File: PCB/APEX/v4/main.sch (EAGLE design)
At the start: 24 parts

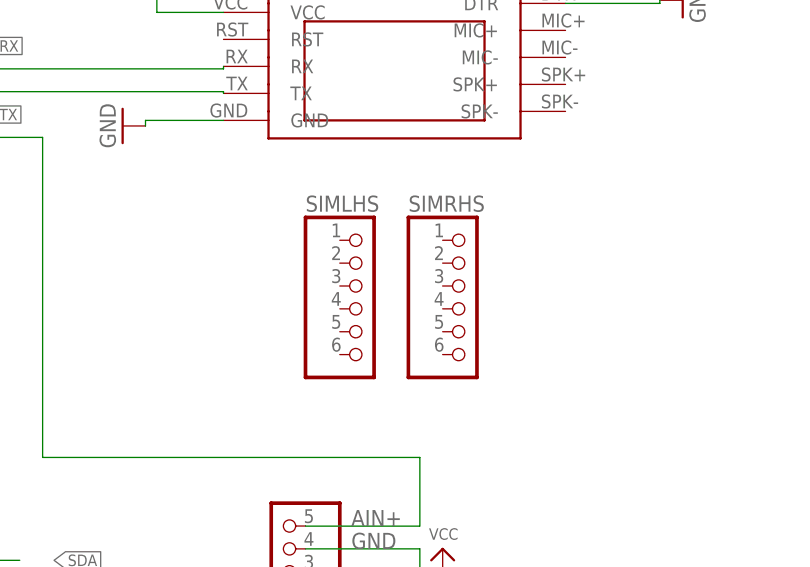
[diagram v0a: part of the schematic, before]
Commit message: use drc to increase pad size
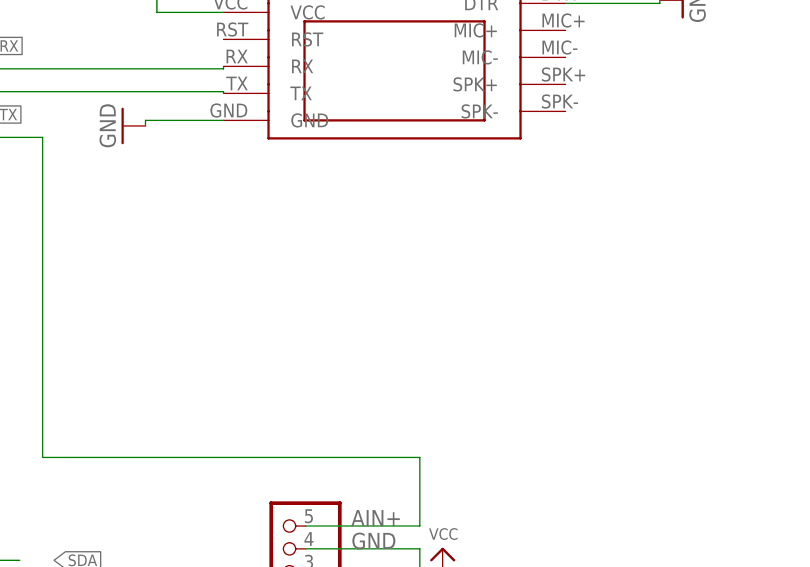
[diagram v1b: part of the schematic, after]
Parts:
- removed SIMLHS, SIMRHS: (no value), pinhead:PINHD-1X6
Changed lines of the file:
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@@
 <part name="TINYLHS" library="pinhead" library_urn="urn:adsk.eagle:library:325" deviceset="PINHD-1X8" device="" package3d_urn="urn:adsk.eagle:package:22409/2"/>
 <part name="TINYRHS" library="pinhead" library_urn="urn:adsk.eagle:library:325" deviceset="PINHD-1X8" device="" package3d_urn="urn:adsk.eagle:package:22409/2"/>
-<part name="SIMLHS" library="pinhead" library_urn="urn:adsk.eagle:library:325" deviceset="PINHD-1X6" device="" package3d_urn="urn:adsk.eagle:package:22472/2"/>
-<part name="SIMRHS" library="pinhead" library_urn="urn:adsk.eagle:library:325" deviceset="PINHD-1X6" device="" package3d_urn="urn:adsk.eagle:package:22472/2"/>
 <part name="EXTV+" library="wirepad" library_urn="urn:adsk.eagle:library:412" deviceset="SMD5" device="" package3d_urn="urn:adsk.eagle:package:30841/1"/>
 <part name="EXTGND" library="wirepad" library_urn="urn:adsk.eagle:library:412" deviceset="SMD5" device="" package3d_urn="urn:adsk.eagle:package:30841/1"/>
@@
 <attribute name="VALUE" x="-6.35" y="45.72" size="1.778" layer="96"/>
 </instance>
-<instance part="SIMLHS" gate="A" x="95.25" y="33.02" smashed="yes">
-<attribute name="NAME" x="88.9" y="43.815" size="1.778" layer="95"/>
-<attribute name="VALUE" x="88.9" y="22.86" size="1.778" layer="96"/>
-</instance>
-<instance part="SIMRHS" gate="A" x="106.68" y="33.02" smashed="yes">
-<attribute name="NAME" x="100.33" y="43.815" size="1.778" layer="95"/>
-<attribute name="VALUE" x="100.33" y="22.86" size="1.778" layer="96"/>
-</instance>
 <instance part="EXTV+" gate="1" x="-21.59" y="17.78" smashed="yes">

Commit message: transfer changes to parent file
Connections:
- net AIN+: now also TINYLHS.8
- net GND: now also TINYRHS.2, TINYRHS.8
- net RX: now also TINYLHS.5
- net SCL: now also TINYRHS.6
- net SDA: now also TINYRHS.7
- net TX: now also TINYLHS.6
- net VCC: now also TINYRHS.1
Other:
- moved on the sheet: TINYLHS, TINYRHS
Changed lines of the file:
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@@
 <setting verticaltext="up"/>
 </settings>
-<grid distance="0.05" unitdist="inch" unit="inch" style="lines" multiple="1" display="yes" altdistance="0.005" altunitdist="inch" altunit="inch"/>
+<grid distance="0.1" unitdist="inch" unit="inch" style="lines" multiple="1" display="no" altdistance="0.01" altunitdist="inch" altunit="inch"/>
 <layers>
 <layer number="1" name="Top" color="4" fill="1" visible="no" active="no"/>
@@
 <attribute name="VALUE" x="-1.27" y="80.01" size="1.778" layer="96"/>
 </instance>
-<instance part="TINYLHS" gate="A" x="-10.16" y="58.42" smashed="yes">
-<attribute name="NAME" x="-16.51" y="71.755" size="1.778" layer="95"/>
-<attribute name="VALUE" x="-16.51" y="45.72" size="1.778" layer="96"/>
-</instance>
-<instance part="TINYRHS" gate="A" x="0" y="58.42" smashed="yes">
-<attribute name="NAME" x="-6.35" y="71.755" size="1.778" layer="95"/>
-<attribute name="VALUE" x="-6.35" y="45.72" size="1.778" layer="96"/>
+<instance part="TINYLHS" gate="A" x="115.57" y="29.21" smashed="yes">
+<attribute name="NAME" x="109.22" y="42.545" size="1.778" layer="95"/>
+<attribute name="VALUE" x="109.22" y="16.51" size="1.778" layer="96"/>
+</instance>
+<instance part="TINYRHS" gate="A" x="-21.59" y="58.42" smashed="yes">
+<attribute name="NAME" x="-27.94" y="71.755" size="1.778" layer="95"/>
+<attribute name="VALUE" x="-27.94" y="45.72" size="1.778" layer="96"/>
 </instance>
 <instance part="EXTV+" gate="1" x="-21.59" y="17.78" smashed="yes">
@@
 <wire x1="231.14" y1="13.97" x2="242.57" y2="13.97" width="0.1524" layer="91"/>
 </segment>
+<segment>
+<pinref part="TINYRHS" gate="A" pin="1"/>
+<wire x1="-24.13" y1="68.58" x2="-34.29" y2="68.58" width="0.1524" layer="91"/>
+<label x="-39.37" y="68.58" size="1.27" layer="95" rot="R180" xref="yes"/>
+</segment>
 </net>
 <net name="GND" class="0">
@@
 <wire x1="231.14" y1="7.62" x2="242.57" y2="7.62" width="0.1524" layer="91"/>
 </segment>
+<segment>
+<pinref part="TINYRHS" gate="A" pin="2"/>
+<wire x1="-24.13" y1="66.04" x2="-34.29" y2="66.04" width="0.1524" layer="91"/>
+<label x="-39.37" y="64.77" size="1.27" layer="95" rot="R180" xref="yes"/>
+</segment>
+<segment>
+<pinref part="TINYRHS" gate="A" pin="8"/>
+<wire x1="-24.13" y1="50.8" x2="-34.29" y2="50.8" width="0.1524" layer="91"/>
+<label x="-39.37" y="49.53" size="1.27" layer="95" rot="R180" xref="yes"/>
+</segment>
 </net>
 <net name="AIN+" class="0">
@@
 <wire x1="59.69" y1="52.07" x2="59.69" y2="16.51" width="0.1524" layer="91"/>
 <wire x1="59.69" y1="16.51" x2="101.6" y2="16.51" width="0.1524" layer="91"/>
+<wire x1="101.6" y1="16.51" x2="101.6" y2="21.59" width="0.1524" layer="91"/>
+<junction x="101.6" y="16.51"/>
+<pinref part="TINYLHS" gate="A" pin="8"/>
+<wire x1="101.6" y1="21.59" x2="113.03" y2="21.59" width="0.1524" layer="91"/>
 </segment>
 </net>
@@
 <label x="53.34" y="54.61" size="1.27" layer="95" xref="yes"/>
 </segment>
+<segment>
+<pinref part="TINYLHS" gate="A" pin="6"/>
+<wire x1="113.03" y1="26.67" x2="97.79" y2="26.67" width="0.1524" layer="91"/>
+<label x="93.98" y="26.67" size="1.27" layer="95" rot="R180" xref="yes"/>
+</segment>
 </net>
 <net name="RX" class="0">
@@
 <label x="53.34" y="62.23" size="1.27" layer="95" xref="yes"/>
 </segment>
+<segment>
+<pinref part="TINYLHS" gate="A" pin="5"/>
+<wire x1="113.03" y1="29.21" x2="97.79" y2="29.21" width="0.1524" layer="91"/>
+<label x="97.79" y="30.48" size="1.27" layer="95" rot="R90" xref="yes"/>
+</segment>
 </net>
 <net name="SDA" class="0">
@@
 <label x="252.73" y="-5.08" size="1.27" layer="95" xref="yes"/>
 </segment>
+<segment>
+<pinref part="TINYRHS" gate="A" pin="7"/>
+<wire x1="-24.13" y1="53.34" x2="-34.29" y2="53.34" width="0.1524" layer="91"/>
+<label x="-39.37" y="53.34" size="1.27" layer="95" rot="R180" xref="yes"/>
+</segment>
 </net>
 <net name="SCL" class="0">
@@
 <label x="252.73" y="1.27" size="1.27" layer="95" xref="yes"/>
 </segment>
+<segment>
+<pinref part="TINYRHS" gate="A" pin="6"/>
+<wire x1="-24.13" y1="55.88" x2="-34.29" y2="55.88" width="0.1524" layer="91"/>
+<label x="-39.37" y="57.15" size="1.27" layer="95" rot="R180" xref="yes"/>
+</segment>
 </net>

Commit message: backport changes to parent design
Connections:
- net SIMPOW: now also U$1.RST
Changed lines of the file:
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@@
 <label x="76.2" y="77.47" size="1.27" layer="95" xref="yes"/>
+</segment>
+<segment>
+<pinref part="U$1" gate="G$1" pin="RST"/>
+<wire x1="79.79" y1="62.96" x2="68.58" y2="62.96" width="0.1524" layer="91"/>
+<wire x1="68.58" y1="62.96" x2="68.58" y2="73.66" width="0.1524" layer="91"/>
+<label x="66.04" y="73.66" size="1.27" layer="95" rot="R180" xref="yes"/>
 </segment>
 </net>
